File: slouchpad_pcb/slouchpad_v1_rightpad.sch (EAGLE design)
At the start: 10 parts

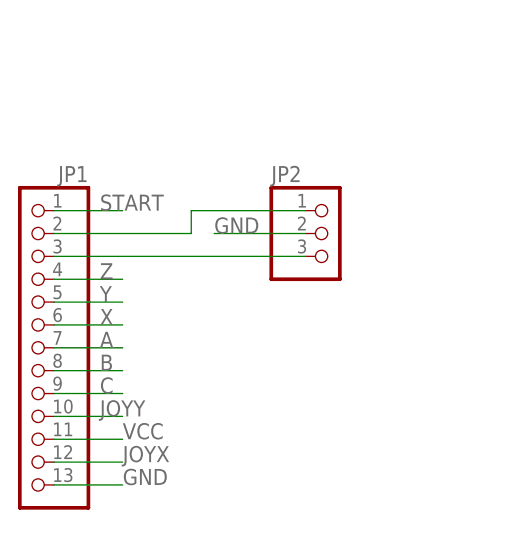
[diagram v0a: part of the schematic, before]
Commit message: Retooled the project to be a modular joypad
Rather than being a shield for the SparkFun Pro Micro Arduino, the slouchpad will simply be a modular joypad for use with any microcontroller.

Modified the license to reflect the removal of the SparkFun Pro Micro

Removed backup design files

Created button layout for left thumb pad

Modified all board positions to units of mm where possible.

Signed-off-by: Eric Jones <eric.r.k.jones@gmail.com>
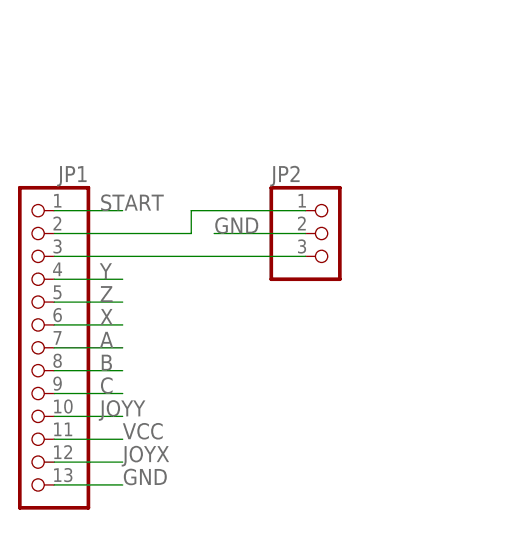
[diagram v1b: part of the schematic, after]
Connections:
- net Y: now also JP1.4; no longer JP1.5
- net Z: now also JP1.5; no longer JP1.4
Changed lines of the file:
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@@
 </segment>
 <segment>
-<pinref part="JP1" gate="A" pin="5"/>
-<wire x1="-22.86" y1="5.08" x2="-15.24" y2="5.08" width="0.1524" layer="91"/>
-<label x="-17.78" y="5.08" size="1.778" layer="95"/>
+<pinref part="JP1" gate="A" pin="4"/>
+<wire x1="-22.86" y1="7.62" x2="-15.24" y2="7.62" width="0.1524" layer="91"/>
+<label x="-17.78" y="7.62" size="1.778" layer="95"/>
 </segment>
 </net>
@@
 </segment>
 <segment>
-<pinref part="JP1" gate="A" pin="4"/>
-<wire x1="-22.86" y1="7.62" x2="-15.24" y2="7.62" width="0.1524" layer="91"/>
-<label x="-17.78" y="7.62" size="1.778" layer="95"/>
+<pinref part="JP1" gate="A" pin="5"/>
+<wire x1="-22.86" y1="5.08" x2="-15.24" y2="5.08" width="0.1524" layer="91"/>
+<label x="-17.78" y="5.08" size="1.778" layer="95"/>
 </segment>
 </net>
